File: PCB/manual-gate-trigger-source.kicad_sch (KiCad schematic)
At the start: 0 parts

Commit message: :sparkles: Draft a trigger input
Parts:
- added D?: 1N4148, Diode_THT:D_DO-35_SOD27_P7.62mm_Horizontal, symbol Diode:1N4148
- added J?: AudioJack2, symbol Connector:AudioJack2
- added Q?: BC547, Package_TO_SOT_THT:TO-92_Inline, symbol Transistor_BJT:BC547
- added R? (x3): 10k, symbol Device:R
- added SW?: SW_Push, symbol Switch:SW_Push
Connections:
- new net: D?.1 (K), Q?.2 (B), R?.2, R?.2
- new net: R?.1, SW?.2
- new net: J?.T, R?.1
- new net +12V: R?.2, SW?.1
- new net GND: D?.2 (A), J?.S, Q?.3 (E)
- new net TRIGGER_IN: Q?.1 (C), R?.1

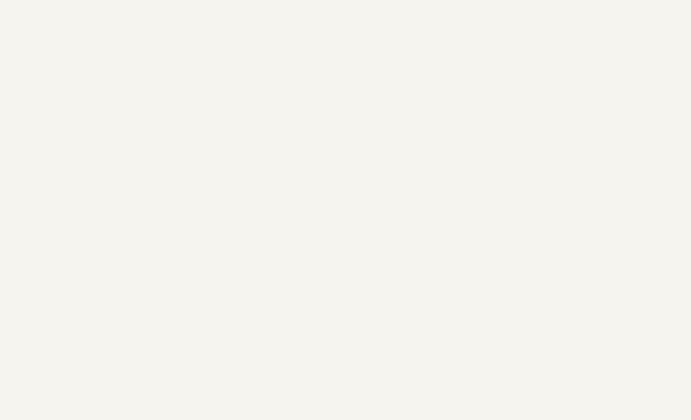
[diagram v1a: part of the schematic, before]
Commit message: :sparkles: Draft a trigger output
Based on http://www.synthpanel.com/modules/cgs24_gatetotrigger.html

Fixes #1
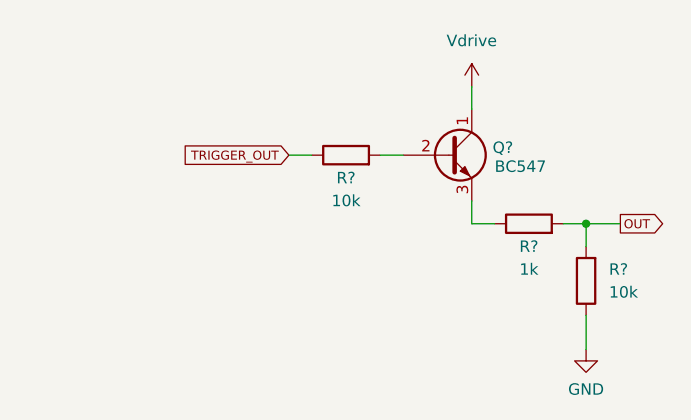
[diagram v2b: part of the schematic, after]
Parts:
- added Q?: BC547, Package_TO_SOT_THT:TO-92_Inline, symbol Transistor_BJT:BC547
- added R? (x2): 10k, symbol Device:R
- added R?: 1k, symbol Device:R
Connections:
- net GND: now also R?.1
- new net: Q?.2 (B), R?.2
- new net: Q?.3 (E), R?.1
- new net OUT: R?.2, R?.2
- new net TRIGGER_OUT: R?.1
- new net Vdrive: Q?.1 (C)
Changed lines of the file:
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@@
   (junction (at 50.8 128.27) (diameter 0) (color 0 0 0 0)
   )
+  (junction (at 259.08 128.27) (diameter 0) (color 0 0 0 0)
+  )
+  (wire (pts (xy 236.22 120.65) (xy 238.76 120.65))
+    (stroke (width 0) (type default) (color 0 0 0 0))
+  )
   (wire (pts (xy 35.56 128.27) (xy 40.64 128.27))
     (stroke (width 0) (type default) (color 0 0 0 0))
@@
     (stroke (width 0) (type default) (color 0 0 0 0))
   )
+  (wire (pts (xy 246.38 128.27) (xy 248.92 128.27))
+    (stroke (width 0) (type default) (color 0 0 0 0))
+  )
   (wire (pts (xy 48.26 128.27) (xy 50.8 128.27))
     (stroke (width 0) (type default) (color 0 0 0 0))
@@
     (stroke (width 0) (type default) (color 0 0 0 0))
   )
+  (wire (pts (xy 246.38 125.73) (xy 246.38 128.27))
+    (stroke (width 0) (type default) (color 0 0 0 0))
+  )
+  (wire (pts (xy 226.06 120.65) (xy 228.6 120.65))
+    (stroke (width 0) (type default) (color 0 0 0 0))
+  )
   (wire (pts (xy 58.42 120.65) (xy 58.42 123.19))
     (stroke (width 0) (type default) (color 0 0 0 0))
   )
+  (wire (pts (xy 259.08 128.27) (xy 262.89 128.27))
+    (stroke (width 0) (type default) (color 0 0 0 0))
+  )
   (wire (pts (xy 58.42 120.65) (xy 62.23 120.65))
     (stroke (width 0) (type default) (color 0 0 0 0))
@@
     (stroke (width 0) (type default) (color 0 0 0 0))
   )
+  (wire (pts (xy 259.08 128.27) (xy 259.08 130.81))
+    (stroke (width 0) (type default) (color 0 0 0 0))
+  )
   (wire (pts (xy 50.8 128.27) (xy 50.8 135.89))
     (stroke (width 0) (type default) (color 0 0 0 0))
   )
+  (wire (pts (xy 259.08 138.43) (xy 259.08 142.24))
+    (stroke (width 0) (type default) (color 0 0 0 0))
+  )
   (wire (pts (xy 58.42 135.89) (xy 58.42 138.43))
     (stroke (width 0) (type default) (color 0 0 0 0))
@@
   )
   (wire (pts (xy 58.42 133.35) (xy 58.42 135.89))
+    (stroke (width 0) (type default) (color 0 0 0 0))
+  )
+  (wire (pts (xy 246.38 113.03) (xy 246.38 115.57))
+    (stroke (width 0) (type default) (color 0 0 0 0))
+  )
+  (wire (pts (xy 256.54 128.27) (xy 259.08 128.27))
     (stroke (width 0) (type default) (color 0 0 0 0))
   )
@@
     )
   )
+  (global_label "TRIGGER_OUT" (shape input) (at 226.06 120.65 180) (fields_autoplaced)
+    (effects (font (size 1 1)) (justify right))
+    (property "Intersheet References" "${INTERSHEET_REFS}" (id 0) (at 214.3981 120.5875 0)
+      (effects (font (size 1 1)) (justify right) hide)
+    )
+  )
+  (global_label "OUT" (shape output) (at 262.89 128.27 0) (fields_autoplaced)
+    (effects (font (size 1 1)) (justify left))
+    (property "Intersheet References" "${INTERSHEET_REFS}" (id 0) (at 267.6471 128.2075 0)
+      (effects (font (size 1 1)) (justify left) hide)
+    )
+  )
+  (symbol (lib_id "Transistor_BJT:BC547") (at 243.84 120.65 0) (unit 1)
+    (in_bom yes) (on_board yes)
+    (property "Reference" "Q?" (id 0) (at 248.6914 119.8153 0)
+      (effects (font (size 1.27 1.27)) (justify left))
+    )
+    (property "Value" "BC547" (id 1) (at 248.92 121.92 0)
+      (effects (font (size 1.27 1.27)) (justify left))
+    )
+    (property "Footprint" "Package_TO_SOT_THT:TO-92_Inline" (id 2) (at 248.92 122.555 0)
+      (effects (font (size 1.27 1.27) italic) (justify left) hide)
+    )
+    (property "Datasheet" "https://www.onsemi.com/pub/Collateral/BC550-D.pdf" (id 3) (at 243.84 120.65 0)
+      (effects (font (size 1.27 1.27)) (justify left) hide)
+    )
+    (pin "1")
+    (pin "2")
+    (pin "3")
+  )
+  (symbol (lib_id "power:GND") (at 259.08 142.24 0) (unit 1)
+    (in_bom yes) (on_board yes) (fields_autoplaced)
+    (property "Reference" "#PWR?" (id 0) (at 259.08 148.59 0)
+      (effects (font (size 1.27 1.27)) hide)
+    )
+    (property "Value" "GND" (id 1) (at 259.08 146.6834 0))
+    (property "Footprint" "" (id 2) (at 259.08 142.24 0)
+      (effects (font (size 1.27 1.27)) hide)
+    )
+    (property "Datasheet" "" (id 3) (at 259.08 142.24 0)
+      (effects (font (size 1.27 1.27)) hide)
+    )
+    (pin "1")
+  )
   (symbol (lib_id "Transistor_BJT:BC547") (at 55.88 128.27 0) (unit 1)
     (in_bom yes) (on_board yes) (fields_autoplaced)
@@
     (pin "1")
   )
+  (symbol (lib_id "power:Vdrive") (at 246.38 113.03 0) (unit 1)
+    (in_bom yes) (on_board yes) (fields_autoplaced)
+    (property "Reference" "#PWR?" (id 0) (at 241.3 116.84 0)
+      (effects (font (size 1.27 1.27)) hide)
+    )
+    (property "Value" "Vdrive" (id 1) (at 246.38 107.95 0))
+    (property "Footprint" "" (id 2) (at 246.38 113.03 0)
+      (effects (font (size 1.27 1.27)) hide)
+    )
+    (property "Datasheet" "" (id 3) (at 246.38 113.03 0)
+      (effects (font (size 1.27 1.27)) hide)
+    )
+    (pin "1")
+  )
   (symbol (lib_id "power:GND") (at 36.83 137.16 0) (unit 1)
     (in_bom yes) (on_board yes) (fields_autoplaced)
@@
     )
     (pin "1")
+  )
+  (symbol (lib_id "Device:R") (at 259.08 134.62 180) (unit 1)
+    (in_bom yes) (on_board yes) (fields_autoplaced)
+    (property "Reference" "R?" (id 0) (at 261.62 133.3499 0)
+      (effects (font (size 1.27 1.27)) (justify right))
+    )
+    (property "Value" "10k" (id 1) (at 261.62 135.8899 0)
+      (effects (font (size 1.27 1.27)) (justify right))
+    )
+    (property "Footprint" "" (id 2) (at 260.858 134.62 90)
+      (effects (font (size 1.27 1.27)) hide)
+    )
+    (property "Datasheet" "~" (id 3) (at 259.08 134.62 0)
+      (effects (font (size 1.27 1.27)) hide)
+    )
+    (pin "1")
+    (pin "2")
   )
   (symbol (lib_id "Diode:1N4148") (at 54.61 135.89 0) (unit 1)
@@
     (pin "2")
   )
+  (symbol (lib_id "Device:R") (at 232.41 120.65 90) (unit 1)
+    (in_bom yes) (on_board yes)
+    (property "Reference" "R?" (id 0) (at 232.41 123.19 90))
+    (property "Value" "10k" (id 1) (at 232.41 125.73 90))
+    (property "Footprint" "" (id 2) (at 232.41 122.428 90)
+      (effects (font (size 1.27 1.27)) hide)
+    )
+    (property "Datasheet" "~" (id 3) (at 232.41 120.65 0)
+      (effects (font (size 1.27 1.27)) hide)
+    )
+    (pin "1")
+    (pin "2")
+  )
   (symbol (lib_id "Switch:SW_Push") (at 31.75 115.57 0) (unit 1)
     (in_bom yes) (on_board yes) (fields_autoplaced)
@@
     (pin "1")
   )
+  (symbol (lib_id "Device:R") (at 252.73 128.27 90) (unit 1)
+    (in_bom yes) (on_board yes)
+    (property "Reference" "R?" (id 0) (at 252.73 130.81 90))
+    (property "Value" "1k" (id 1) (at 252.73 133.35 90))
+    (property "Footprint" "" (id 2) (at 252.73 130.048 90)
+      (effects (font (size 1.27 1.27)) hide)
+    )
+    (property "Datasheet" "~" (id 3) (at 252.73 128.27 0)
+      (effects (font (size 1.27 1.27)) hide)
+    )
+    (pin "1")
+    (pin "2")
+  )
   (symbol (lib_id "Device:R") (at 44.45 128.27 90) (unit 1)
     (in_bom yes) (on_board yes) (fields_autoplaced)
@@
   )
   (symbol_instances
+    (path "/22c0a682-9532-4c74-84e6-cd37a121d21b"
+      (reference "#PWR?") (unit 1) (value "GND") (footprint "")
+    )
     (path "/23ea411a-ad60-438b-bff0-975e4087c521"
       (reference "#PWR?") (unit 1) (value "+12V") (footprint "")
@@
       (reference "#PWR?") (unit 1) (value "GND") (footprint "")
     )
+    (path "/64ad730c-661f-432d-bffe-a373f6bdcd59"
+      (reference "#PWR?") (unit 1) (value "Vdrive") (footprint "")
+    )
     (path "/6d1f2f89-eaba-45e9-ae14-f34667c030d8"
       (reference "#PWR?") (unit 1) (value "GND") (footprint "")
@@
       (reference "J?") (unit 1) (value "AudioJack2") (footprint "")
     )
+    (path "/0a4bdb17-476b-4702-8de8-f7da8cd8459d"
+      (reference "Q?") (unit 1) (value "BC547") (footprint "Package_TO_SOT_THT:TO-92_Inline")
+    )
     (path "/22fb94c8-6b29-495d-9a76-5cf3140e61ad"
       (reference "Q?") (unit 1) (value "BC547") (footprint "Package_TO_SOT_THT:TO-92_Inline")
@@
       (reference "R?") (unit 1) (value "10k") (footprint "")
     )
+    (path "/6ed9684c-05ae-4df1-9695-18550706cee4"
+      (reference "R?") (unit 1) (value "10k") (footprint "")
+    )
+    (path "/883a8c4d-f760-4d51-b2a5-2407fbd59bc7"
+      (reference "R?") (unit 1) (value "10k") (footprint "")
+    )
+    (path "/c7af4d99-9e2b-4d8a-80e7-cea49430b108"
+      (reference "R?") (unit 1) (value "1k") (footprint "")
+    )
     (path "/ceca7e89-cc8e-4e4d-a7a5-87d63d1be391"

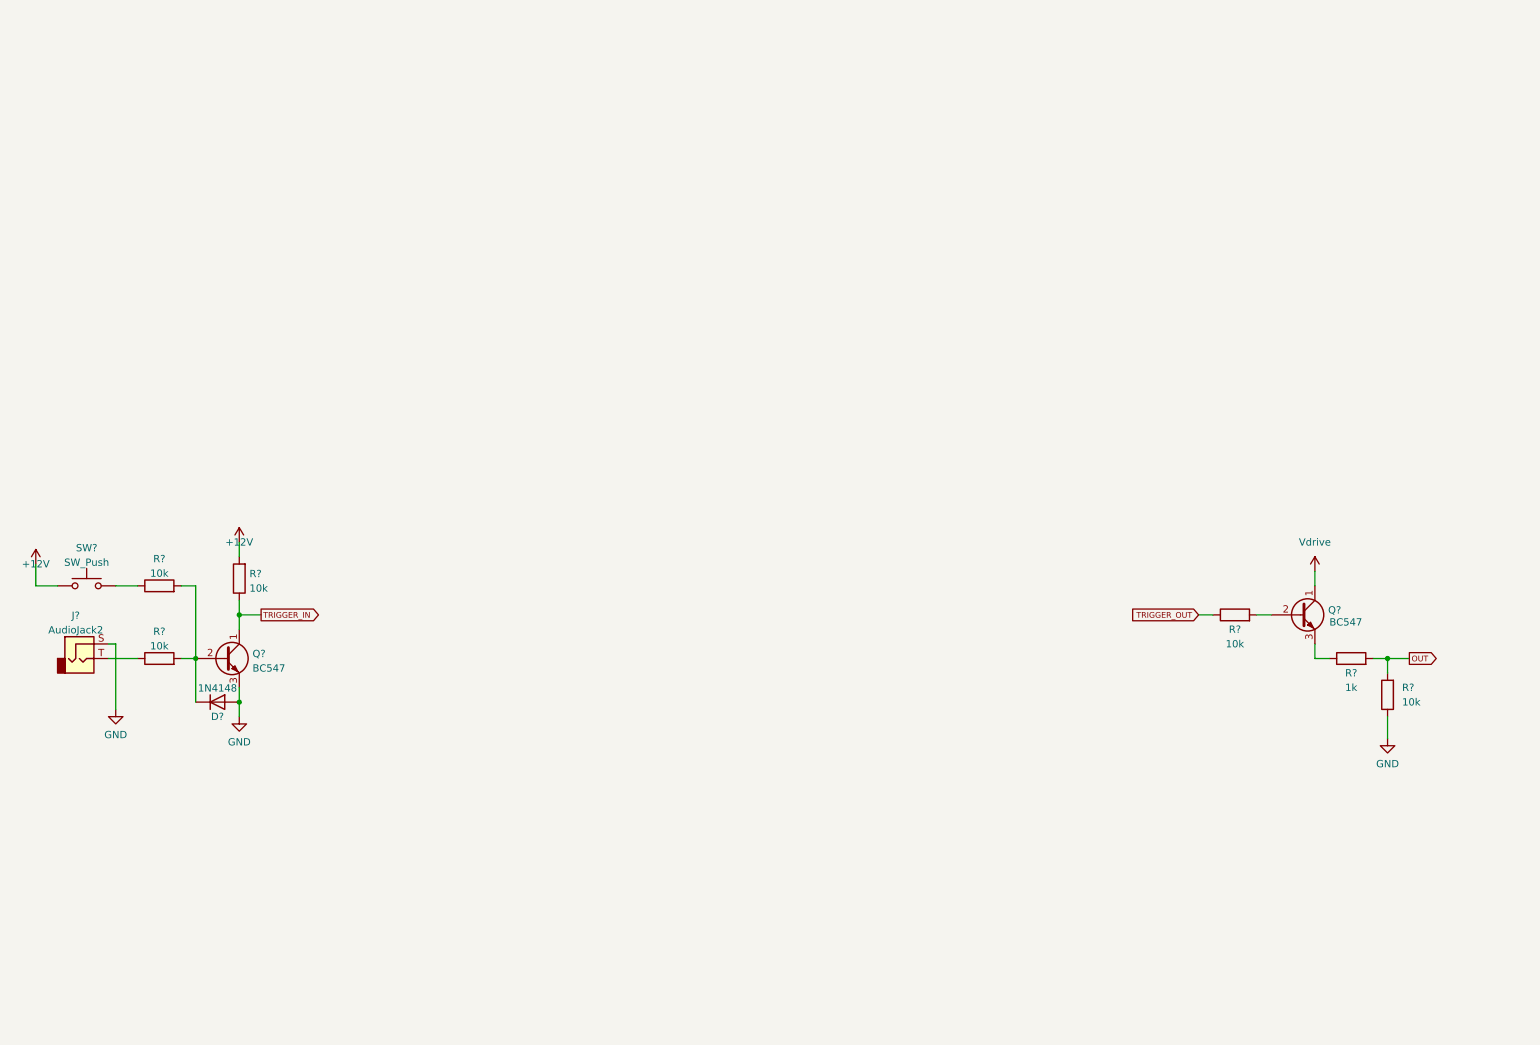
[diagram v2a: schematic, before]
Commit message: :sparkles: Add OPV-based voltage generation and selector
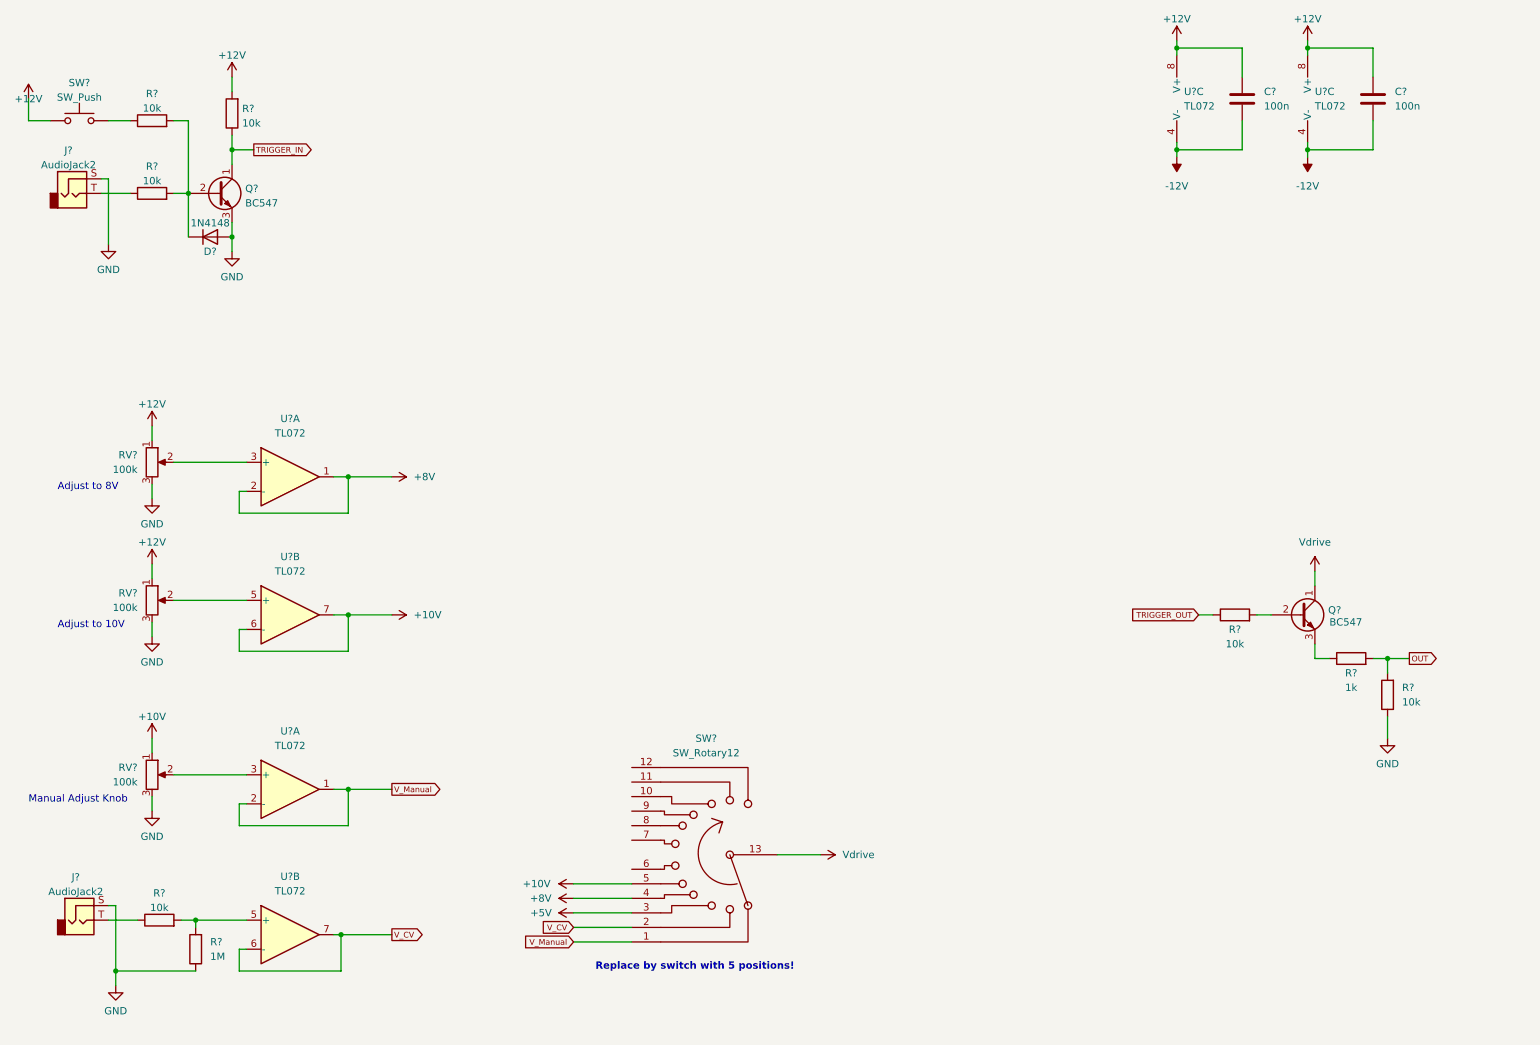
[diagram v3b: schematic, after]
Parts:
- added C? (x2): 100n, symbol Device:C
- added J?: AudioJack2, symbol Connector:AudioJack2
- added R?: 1M, symbol Device:R
- added R?: 10k, symbol Device:R
- added RV? (x3): 100k, symbol Device:R_Potentiometer
- added SW?: SW_Rotary12, symbol Switch:SW_Rotary12
- added U? (x6): TL072, symbol Amplifier_Operational:TL072
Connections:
- net +12V: now also C?.1, C?.1, RV?.1, RV?.1, U?.8 (V+), U?.8 (V+)
- net GND: now also J?.S, R?.1, RV?.3, RV?.3, RV?.3
- net Vdrive: now also SW?.13
- new net: R?.2, R?.2, U?.5 (+)
- new net: RV?.2, U?.3 (+) (x2)
- new net: J?.T, R?.1
- new net: RV?.2, U?.5 (+)
- new net +10V: RV?.1, SW?.5, U?.6 (-), U?.7
- new net +5V: SW?.3
- new net +8V: SW?.4, U?.1, U?.2 (-)
- new net -12V: C?.2, C?.2, U?.4 (V-), U?.4 (V-)
- new net V_CV: SW?.2, U?.6 (-), U?.7
- new net V_Manual: SW?.1, U?.1, U?.2 (-)
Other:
- note added: "Adjust to 10V"
- note added: "Adjust to 8V"
- note added: "Manual Adjust Knob"
- note added: "Replace by switch with 5 positions!"
- moved on the sheet: D?, J?, Q?, R?, SW?

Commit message: :art: Change voltage generation to R divider
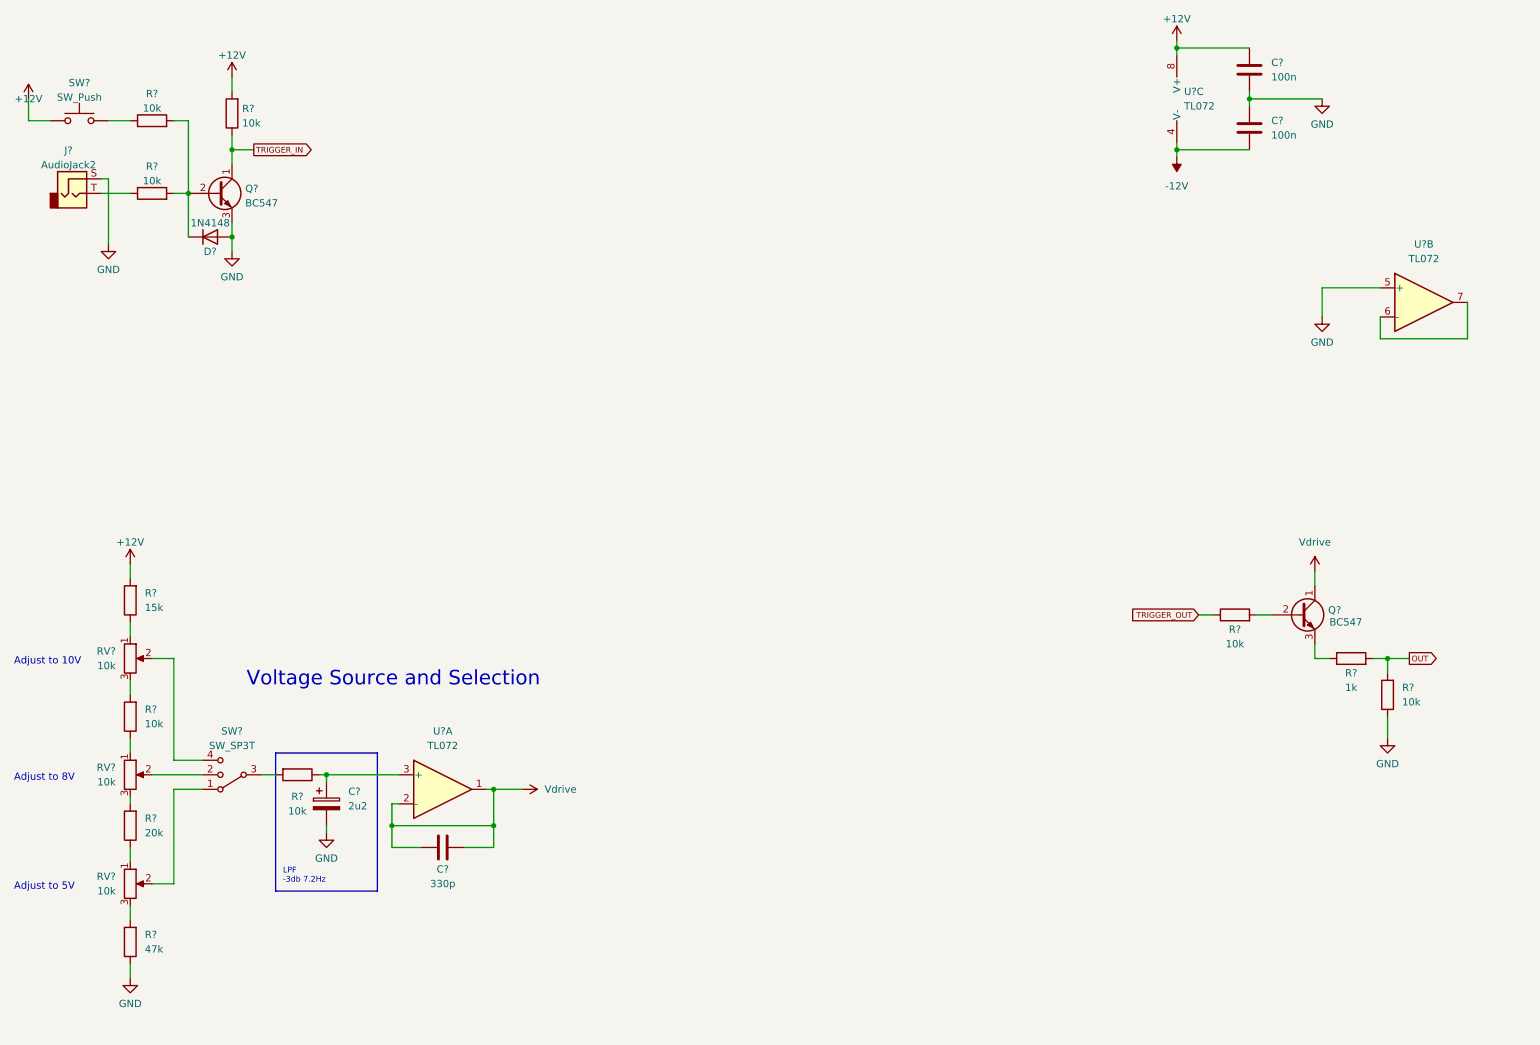
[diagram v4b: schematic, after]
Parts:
- removed C?: 100n, symbol Device:C
- removed J?: AudioJack2, symbol Connector:AudioJack2
- removed R?: 1M, symbol Device:R
- removed R?: 10k, symbol Device:R
- removed RV? (x3): 100k, symbol Device:R_Potentiometer
- removed SW?: SW_Rotary12, symbol Switch:SW_Rotary12
- removed U? (x6): TL072, symbol Amplifier_Operational:TL072
- added C?: 2u2, symbol Device:C_Polarized
- added C?: 100n, symbol Device:C
- added C?: 330p, symbol Device:C
- added R? (x2): 10k, symbol Device:R
- added R?: 15k, symbol Device:R
- added R?: 20k, symbol Device:R
- added R?: 47k, symbol Device:R
- added RV? (x3): 10k, symbol Device:R_Potentiometer
- added SW?: SW_SP3T, symbol Switch:SW_SP3T
- added U? (x3): TL072, symbol Amplifier_Operational:TL072
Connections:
- net +12V: now also R?.2, U?.8 (V+)
- net -12V: now also C?.2, U?.4 (V-); no longer C?.2
- net GND: now also C?.2, C?.1, C?.2, R?.1, U?.5 (+)
- net Vdrive: now also C?.1, C?.2, U?.1, U?.2 (-)
- new net: C?.1, R?.1, U?.3 (+)
- new net: R?.2, SW?.3
- new net: R?.1, RV?.1 (x3)
- new net: RV?.2, SW?.2
- new net: R?.2, RV?.3 (x3)
- new net: U?.6 (-), U?.7
- new net: RV?.2, SW?.1
- new net: RV?.2, SW?.4
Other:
- note added: "Adjust to 5V"
- note added: "LPF -3db 7.2Hz"
- note added: "Voltage Source and Selection"
- note removed: "Manual Adjust Knob"
- note removed: "Replace by switch with 5 positions!"
- moved on the sheet: C?
